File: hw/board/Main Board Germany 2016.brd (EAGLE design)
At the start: 101.6 x 101.3 mm, 62 parts, among them IC1 7805T

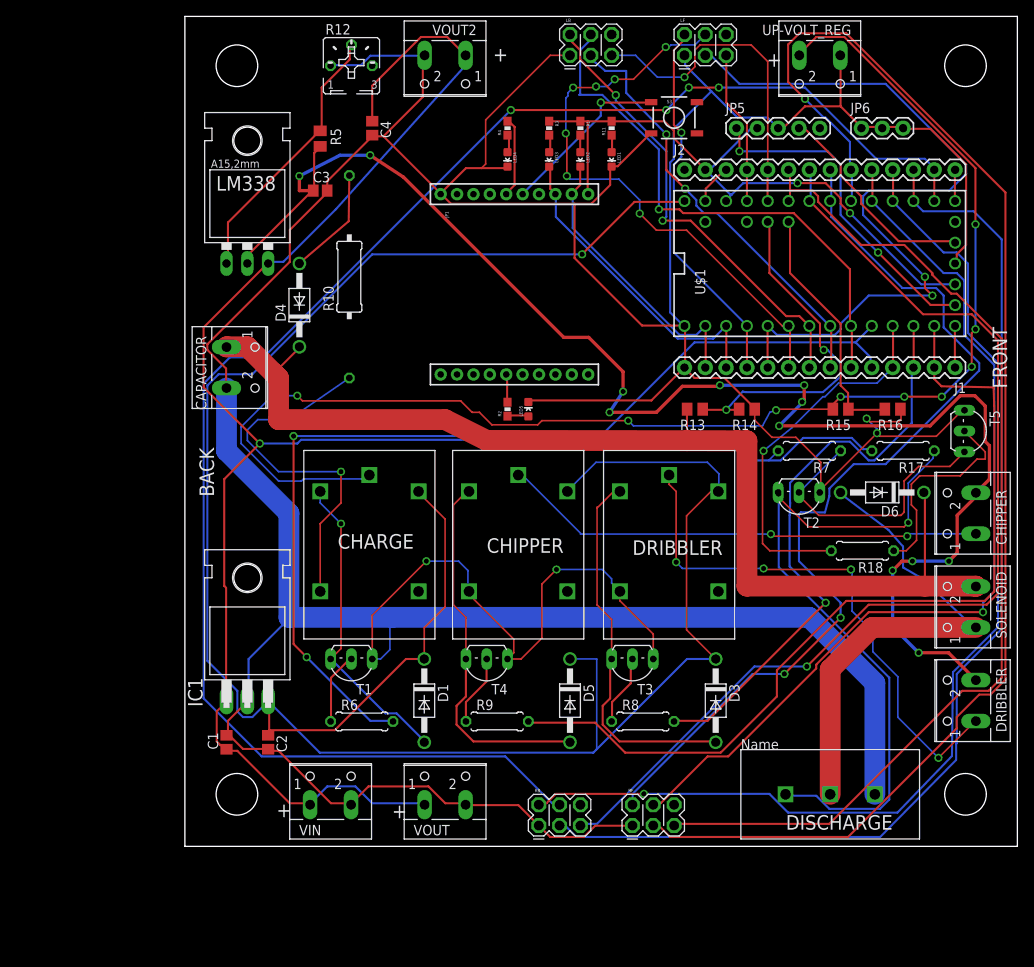
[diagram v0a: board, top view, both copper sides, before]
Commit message: separation in two boards - work in progress
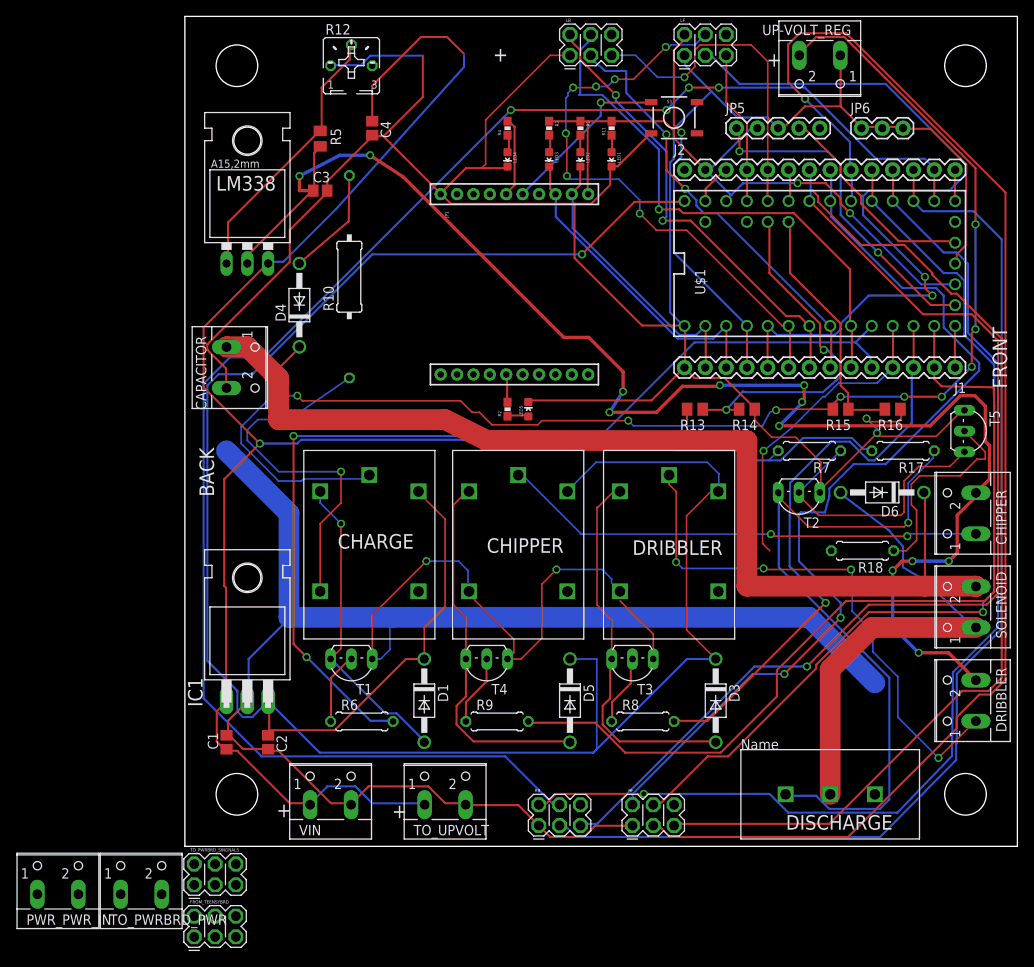
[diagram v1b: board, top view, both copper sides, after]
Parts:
- removed VOUT2: (no value), con-wago-500:W237-102
- added FROM_TEENSYBRD, TO_PWRBRD_SINGNALS: (no value), SparkFun-Connectors:2X3_POGO
- added PWR_PWR_IN, TO_PWRBRD_PWR: (no value), con-wago-500:W237-102
- renumbered VOUT to TO_UPVOLT
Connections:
- new net PWR_CHARGE: FROM_TEENSYBRD.P$5, R6.2
- new net PWR_CHIP: FROM_TEENSYBRD.P$6, R9.2
- new net PWR_DISCHARGE: FROM_TEENSYBRD.P$2, R18.2
- new net PWR_DRIBBLE: FROM_TEENSYBRD.P$4, R8.2
- new net PWR_GND: CAPACITOR.2, T3.E, TO_UPVOLT.2, U$2.EMITTERPAD, U$4.P$4, UP-VOLT_REG.1
- new net PWR_READ_250: FROM_TEENSYBRD.P$1, R15.1, R16.2
- new net PWR_READ_CAP: FROM_TEENSYBRD.P$3, R13.1, R14.2
- new net PWR_VCC: C4.1, LM338.3, TO_UPVOLT.1
- net +24V: now also TO_PWRBRD_PWR.1; no longer C4.1, LM338.3, TO_UPVOLT.1, VOUT2.1
- net CHARGE: now also TO_PWRBRD_SINGNALS.P$5; no longer R6.2
- net CHIP: now also TO_PWRBRD_SINGNALS.P$6; no longer R9.2
- net DISCHARGE: no longer R18.2
- net DRIBBLE: now also TO_PWRBRD_SINGNALS.P$4; no longer R8.2
- net GND: now also TO_PWRBRD_PWR.2; no longer CAPACITOR.2, T3.E, TO_UPVOLT.2, U$2.EMITTERPAD, U$4.P$4, UP-VOLT_REG.1, VOUT2.2
- net READ_250: now also TO_PWRBRD_SINGNALS.P$1; no longer R15.1, R16.2
- net READ_CAP: now also TO_PWRBRD_SINGNALS.P$3; no longer R13.1, R14.2
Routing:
- net +24V: track 231.8 -> 176.0 mm
- net PWR_VCC: track 0.00 -> 54.6 mm
- net GND: track 603.3 -> 569.7 mm
- net PWR_GND: track 0.00 -> 8.79 mm
- net DISCHARGE: track 45.7 -> 38.2 mm
- net READ_250: track 30.4 -> 25.8 mm
- net PWR_READ_250: track 0.00 -> 4.48 mm
